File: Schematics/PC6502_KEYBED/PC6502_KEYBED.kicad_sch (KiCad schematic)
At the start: 30 parts, among them J4 Conn_02x05_Odd_Even, J6 MTJ-88ARX1-FSM-LG, Q7 2N3904, Q8 2N3904, U1 ATmega644P-20P, U2 74HC238, X2 CXO_DIP8

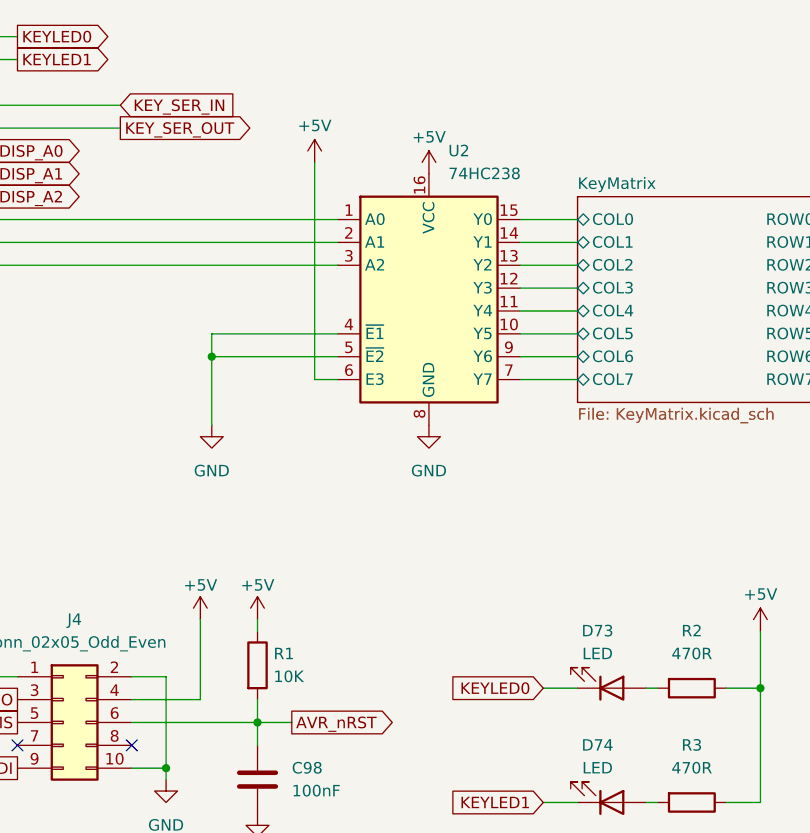
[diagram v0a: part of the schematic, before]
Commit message: Keyboard code and schematics
Updated the Schematics and have a mostly functioning keyboard (can't turn off caps lock yet)
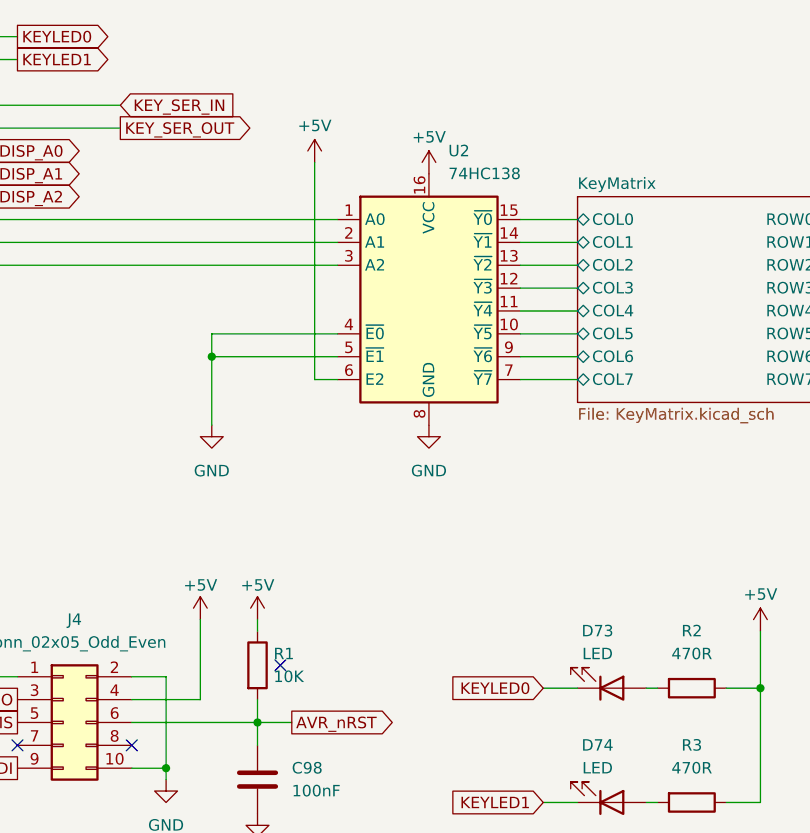
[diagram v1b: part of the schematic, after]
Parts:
- removed U2: 74HC238, Package_DIP:DIP-16_W7.62mm, symbol 74xx:74HC238
- added U2: 74HC138, symbol 74xx:74HC138
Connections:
- net +5V: now also U2.16 (VCC), U2.6 (E2)
- net GND: now also U2.4 (~{E0}), U2.5 (~{E1}), U2.8 (GND)
- net KeyMatrix/COL0: now also U2.15 (~{Y0})
- net KeyMatrix/COL1: now also U2.14 (~{Y1})
- net KeyMatrix/COL2: now also U2.13 (~{Y2})
- net KeyMatrix/COL3: now also U2.12 (~{Y3})
- net KeyMatrix/COL4: now also U2.11 (~{Y4})
- net KeyMatrix/COL5: now also U2.10 (~{Y5})
- net KeyMatrix/COL6: now also U2.9 (~{Y6})
- net KeyMatrix/COL7: now also U2.7 (~{Y7})
- net at U1.19 (PD5): now also U2.1 (A0)
- net at U1.20 (PD6): now also U2.2 (A1)
- net at U1.21 (PD7): now also U2.3 (A2)
- no-connect marks 5 -> 6
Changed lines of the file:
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@@
 	)
 	(no_connect
+		(at 111.76 167.64)
+	)
+	(no_connect
 		(at 95.25 176.53)
 	)
@@
 	)
 	(symbol
-		(lib_id "74xx:74HC238")
-		(at 128.27 128.27 0)
-		(unit 1)
-		(exclude_from_sim no)
-		(in_bom yes)
-		(on_board yes)
-		(dnp no)
-		(fields_autoplaced yes)
-		(property "Reference" "U2"
-			(at 130.4133 110.49 0)
-			(effects
-				(font
-					(size 1.27 1.27)
-				)
-				(justify left)
-			)
-		)
-		(property "Value" "74HC238"
-			(at 130.4133 113.03 0)
-			(effects
-				(font
-					(size 1.27 1.27)
-				)
-				(justify left)
-			)
-		)
-		(property "Footprint" "Package_DIP:DIP-16_W7.62mm"
-			(at 128.27 128.27 0)
-			(effects
-				(font
-					(size 1.27 1.27)
-				)
-				(hide yes)
-			)
-		)
-		(property "Datasheet" "https://www.ti.com/lit/ds/symlink/cd74hc238.pdf"
-			(at 128.27 128.27 0)
-			(effects
-				(font
-					(size 1.27 1.27)
-				)
-				(hide yes)
-			)
-		)
-		(property "Description" "3-to-8 line decoder/multiplexer, DIP-16/SOIC-16/SSOP-16"
-			(at 128.27 128.27 0)
-			(effects
-				(font
-					(size 1.27 1.27)
-				)
-				(hide yes)
-			)
-		)
-		(property "LCSC" "DNF"
-			(at 128.27 128.27 0)
-			(effects
-				(font
-					(size 1.27 1.27)
-				)
-				(hide yes)
-			)
-		)
-		(pin "12"
-		)
-		(pin "11"
-		)
-		(pin "7"
-		)
-		(pin "14"
-		)
-		(pin "13"
-		)
-		(pin "3"
-		)
-		(pin "2"
-		)
-		(pin "1"
-		)
-		(pin "10"
-		)
-		(pin "8"
-		)
-		(pin "9"
-		)
-		(pin "6"
-		)
-		(pin "16"
-		)
-		(pin "5"
-		)
-		(pin "4"
-		)
-		(pin "15"
-		)
-		(instances
-			(project ""
-				(path "/df3f2d3f-c20b-413e-9d55-4328b6be904e"
-					(reference "U2")
-					(unit 1)
-				)
-			)
-		)
-	)
-	(symbol
 		(lib_id "Mechanical:MountingHole_Pad")
 		(at 266.7 152.4 0)
@@
 					(unit 1)
 				)
+			)
+		)
+	)
+	(symbol
+		(lib_id "74xx:74HC138")
+		(at 128.27 128.27 0)
+		(unit 1)
+		(exclude_from_sim no)
+		(in_bom yes)
+		(on_board yes)
+		(dnp no)
+		(fields_autoplaced yes)
+		(property "Reference" "U2"
+			(at 130.4133 110.49 0)
+			(effects
+				(font
+					(size 1.27 1.27)
+				)
+				(justify left)
+			)
+		)
+		(property "Value" "74HC138"
+			(at 130.4133 113.03 0)
+			(effects
+				(font
+					(size 1.27 1.27)
+				)
+				(justify left)
+			)
+		)
+		(property "Footprint" ""
+			(at 128.27 128.27 0)
+			(effects
+				(font
+					(size 1.27 1.27)
+				)
+				(hide yes)
+			)
+		)
+		(property "Datasheet" "http://www.ti.com/lit/ds/symlink/cd74hc238.pdf"
+			(at 128.27 128.27 0)
+			(effects
+				(font
+					(size 1.27 1.27)
+				)
+				(hide yes)
+			)
+		)
+		(property "Description" "3-to-8 line decoder/multiplexer inverting, DIP-16/SOIC-16/SSOP-16"
+			(at 128.27 128.27 0)
+			(effects
+				(font
+					(size 1.27 1.27)
+				)
+				(hide yes)
+			)
+		)
+		(pin "13"
+		)
+		(pin "12"
+		)
+		(pin "10"
+		)
+		(pin "7"
+		)
+		(pin "16"
+		)
+		(pin "9"
+		)
+		(pin "5"
+		)
+		(pin "6"
+		)
+		(pin "4"
+		)
+		(pin "15"
+		)
+		(pin "14"
+		)
+		(pin "8"
+		)
+		(pin "2"
+		)
+		(pin "11"
+		)
+		(pin "1"
+		)
+		(pin "3"
+		)
+		(instances
+			(project ""
+				(path "/df3f2d3f-c20b-413e-9d55-4328b6be904e"
+					(reference "U2")
+					(unit 1)
+				)
